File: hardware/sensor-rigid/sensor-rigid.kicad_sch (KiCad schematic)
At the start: 27 parts, among them J1 Conn_01x05, U1 PCA9546APWR

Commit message: Interrupts and new flex design
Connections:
- net SDA1: now reaches FPC1.3 (SDA1), R8.1, U1.4 (SD0)
- net SCL1: now reaches R9.1, U1.5 (SC0)
- net SCL1: now also FPC1.2 (SCL1); no longer FPC1.4
- net SDA2: now reaches FPC1.7 (SDA2), R6.2, U1.6 (SD1)
- net SCL2: now reaches R7.2, U1.7 (SC1)
- net SCL2: now also FPC1.6 (SCL2); no longer FPC1.8
- net INT1: now reaches D2.3 (COM)
- net INT1: now also FPC1.4 (INT1); no longer FPC1.2
- net INT2: now reaches D3.3 (COM)
- net INT2: now also FPC1.8 (INT2); no longer FPC1.6
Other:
- moved on the sheet: FPC1

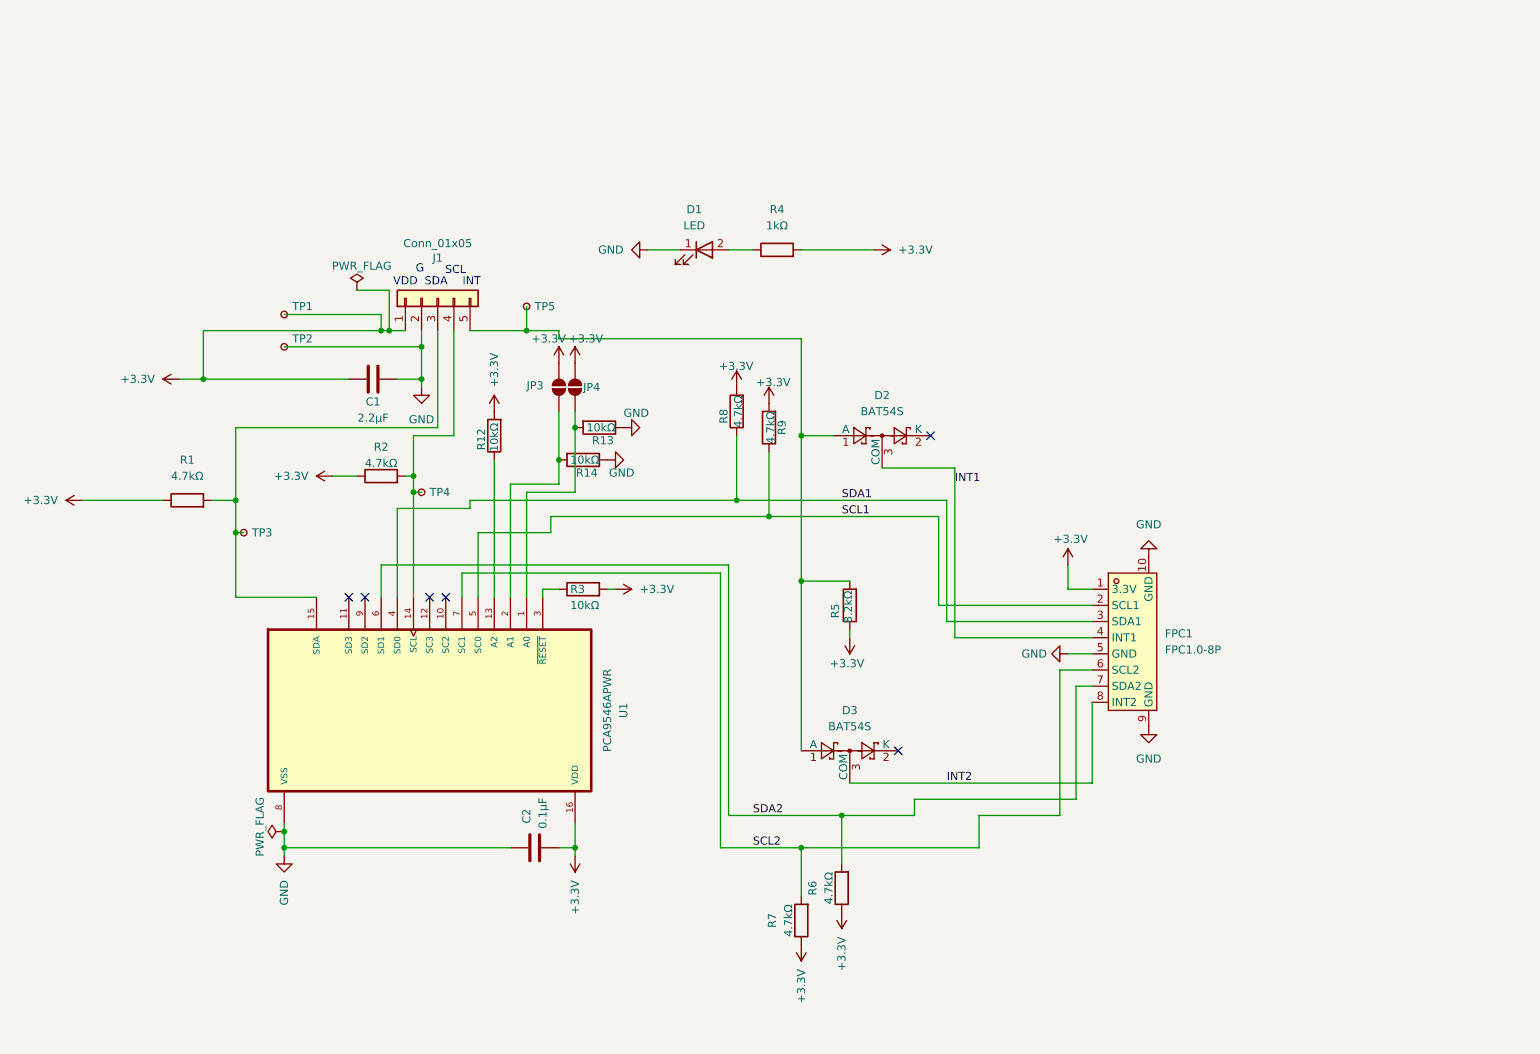
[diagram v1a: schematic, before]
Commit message: Generate circuit-context.json for sensor-rigid and sensor-flex PCBs
Run the existing schematic context extraction and annotation tooling on
both sensor board schematics. Sensor-rigid: 27 components, 16 nets,
6 functional blocks (i2c_mux, connectors, i2c_pull_ups, interrupts,
power, test_points). Sensor-flex: 9 components, 12 nets, 4 blocks
(sensor_1, sensor_2, power, connector). All ai_ properties written to
.kicad_sch files for persistence. Initiative docs and status updates
included.

Made-with: Cursor
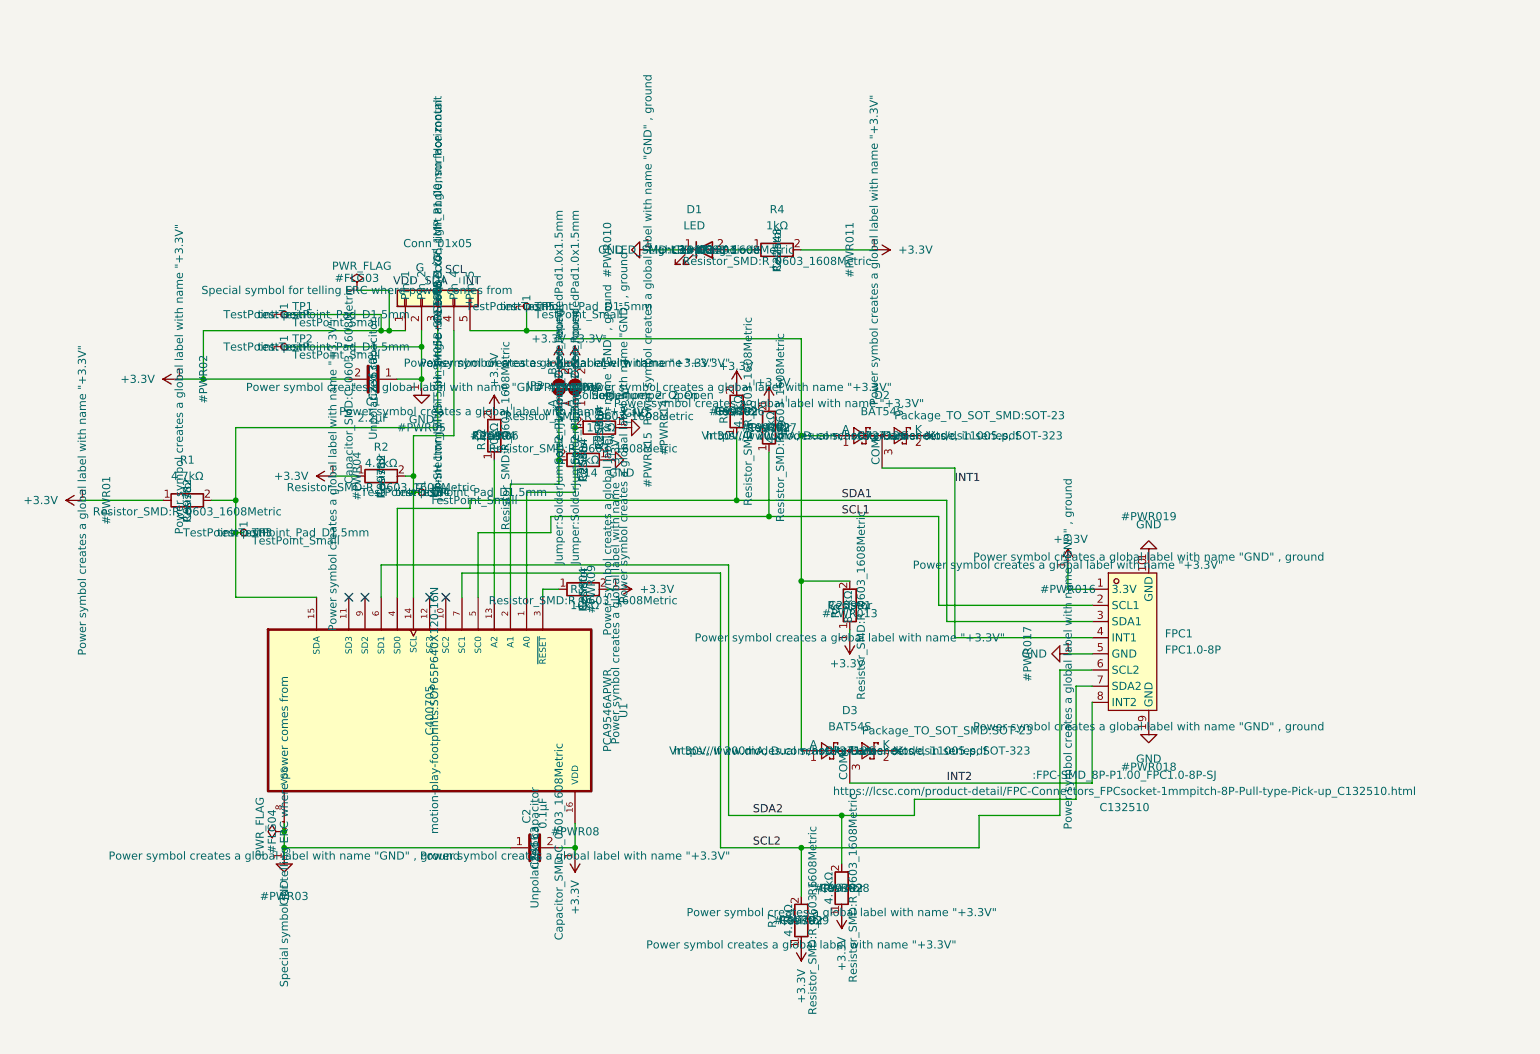
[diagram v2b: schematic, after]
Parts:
- C1: ai_block (none) -> power; ai_critical_specs (none) -> 2.2µF, 0603; ai_function (none) -> Main VDD bypass capacitor; ai_role (none) -> bypass
- C2: ai_block (none) -> power; ai_critical_specs (none) -> 0.1µF, 0603; ai_function (none) -> High-frequency bypass capacitor; ai_role (none) -> bypass
- D1: ai_block (none) -> power; ai_function (none) -> Power indicator LED; ai_role (none) -> indicator
- D2: ai_block (none) -> interrupts; ai_critical_specs (none) -> BAT54S dual Schottky, 200mA; ai_function (none) -> Wired-OR interrupt combiner for sensor 1; ai_role (none) -> diode
- D3: ai_block (none) -> interrupts; ai_critical_specs (none) -> BAT54S dual Schottky, 200mA; ai_function (none) -> Wired-OR interrupt combiner for sensor 2; ai_role (none) -> diode
- FPC1: ai_block (none) -> connectors; ai_critical_specs (none) -> 10-pin, 1.0mm pitch, top contact, slide lock; ai_function (none) -> ZIF FPC connector to flex sensor strip carrying 2x I2C, 2x 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; ai_role (none) -> connector
- J1: ai_block (none) -> connectors; ai_critical_specs (none) -> JST-SH 1mm pitch, 5-pin; ai_function (none) -> 5-pin JST-SH connector to main PCB carrying I2C, power, and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; ai_role (none) -> connector
- JP3: ai_block (none) -> i2c_mux; ai_function (none) -> A1 address select solder jumper — bridge to set A1=1; ai_role (none) -> address_config
- JP4: ai_block (none) -> i2c_mux; ai_function (none) -> A0 address select solder jumper — bridge to set A0=1; ai_role (none) -> address_config
- R1: ai_block (none) -> i2c_pull_ups; ai_critical_specs (none) -> 4.7kΩ to 3.3V; ai_function (none) -> Upstream SDA bus pull-up; ai_role (none) -> pull_up
- R12: ai_block (none) -> i2c_mux; ai_critical_specs (none) -> 10kΩ to 3.3V; ai_function (none) -> A2 address bit pull-up (A2=1 permanent); ai_role (none) -> pull_up
- R13: ai_block (none) -> i2c_mux; ai_critical_specs (none) -> 10kΩ to GND; ai_function (none) -> A0 default pull-down (A0=0 unless JP4 bridged); ai_role (none) -> pull_down
- R14: ai_block (none) -> i2c_mux; ai_critical_specs (none) -> 10kΩ to GND; ai_function (none) -> A1 default pull-down (A1=0 unless JP3 bridged); ai_role (none) -> pull_down
- R2: ai_block (none) -> i2c_pull_ups; ai_critical_specs (none) -> 4.7kΩ to 3.3V; ai_function (none) -> Upstream SCL bus pull-up; ai_role (none) -> pull_up
- R3: ai_block (none) -> i2c_mux; ai_critical_specs (none) -> 10kΩ to 3.3V; ai_function (none) -> Reset pull-up keeping PCA9546A in active state; ai_role (none) -> pull_up
- R4: ai_block (none) -> power; ai_critical_specs (none) -> 1kΩ, ~2.3mA at 3.3V; ai_function (none) -> LED current limiting resistor; ai_role (none) -> current_limit
- R5: ai_block (none) -> interrupts; ai_critical_specs (none) -> 8.2kΩ to 3.3V; ai_function (none) -> Combined INT line pull-up; ai_role (none) -> pull_up
- R6: ai_block (none) -> i2c_pull_ups; ai_critical_specs (none) -> 4.7kΩ to 3.3V; ai_function (none) -> Sensor 2 SDA downstream pull-up; ai_role (none) -> pull_up
- R7: ai_block (none) -> i2c_pull_ups; ai_critical_specs (none) -> 4.7kΩ to 3.3V; ai_function (none) -> Sensor 2 SCL downstream pull-up; ai_role (none) -> pull_up
- R8: ai_block (none) -> i2c_pull_ups; ai_critical_specs (none) -> 4.7kΩ to 3.3V; ai_function (none) -> Sensor 1 SDA downstream pull-up; ai_role (none) -> pull_up
- R9: ai_block (none) -> i2c_pull_ups; ai_critical_specs (none) -> 4.7kΩ to 3.3V; ai_function (none) -> Sensor 1 SCL downstream pull-up; ai_role (none) -> pull_up
- TP1: ai_block (none) -> test_points; ai_function (none) -> 3.3V power rail test point; ai_role (none) -> test_point
- TP2: ai_block (none) -> test_points; ai_function (none) -> GND test point; ai_role (none) -> test_point
- TP3: ai_block (none) -> test_points; ai_function (none) -> Upstream SDA bus test point; ai_role (none) -> test_point
- TP4: ai_block (none) -> test_points; ai_function (none) -> Upstream SCL bus test point; ai_role (none) -> test_point
- TP5: ai_block (none) -> test_points; ai_function (none) -> Combined INT line test point; ai_role (none) -> test_point
- U1: ai_block (none) -> i2c_mux; ai_critical_specs (none) -> PCA9546APWR, 400kHz, address set by A0-A2; ai_function (none) -> 4-channel I2C mux routing upstream bus to 2 downstream sens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; ai_role (none) -> i2c_mux

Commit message: Hardware revision: remove interrupts, update connectors, add DIP switch
Remove INT lines from all three PCBs (main, rigid, flex). Replace 5-pin
JST-SH connectors with 4-pin SM04B-SRSS-TB on main and rigid boards.
Replace solder jumpers with EP-02KS DIP switch for I2C address config
on rigid board. Update FPC connector pinout to remove INT signals and
add GND fills. Update stiffener specs (PI 0.25mm tail, SS 0.2mm IC
areas). Regenerate production files (BOM, CPL) for both sensor boards.
Update hardware CONTEXT.md with corrected addresses (0x74-0x76),
component tables, and pinouts.

Made-with: Cursor
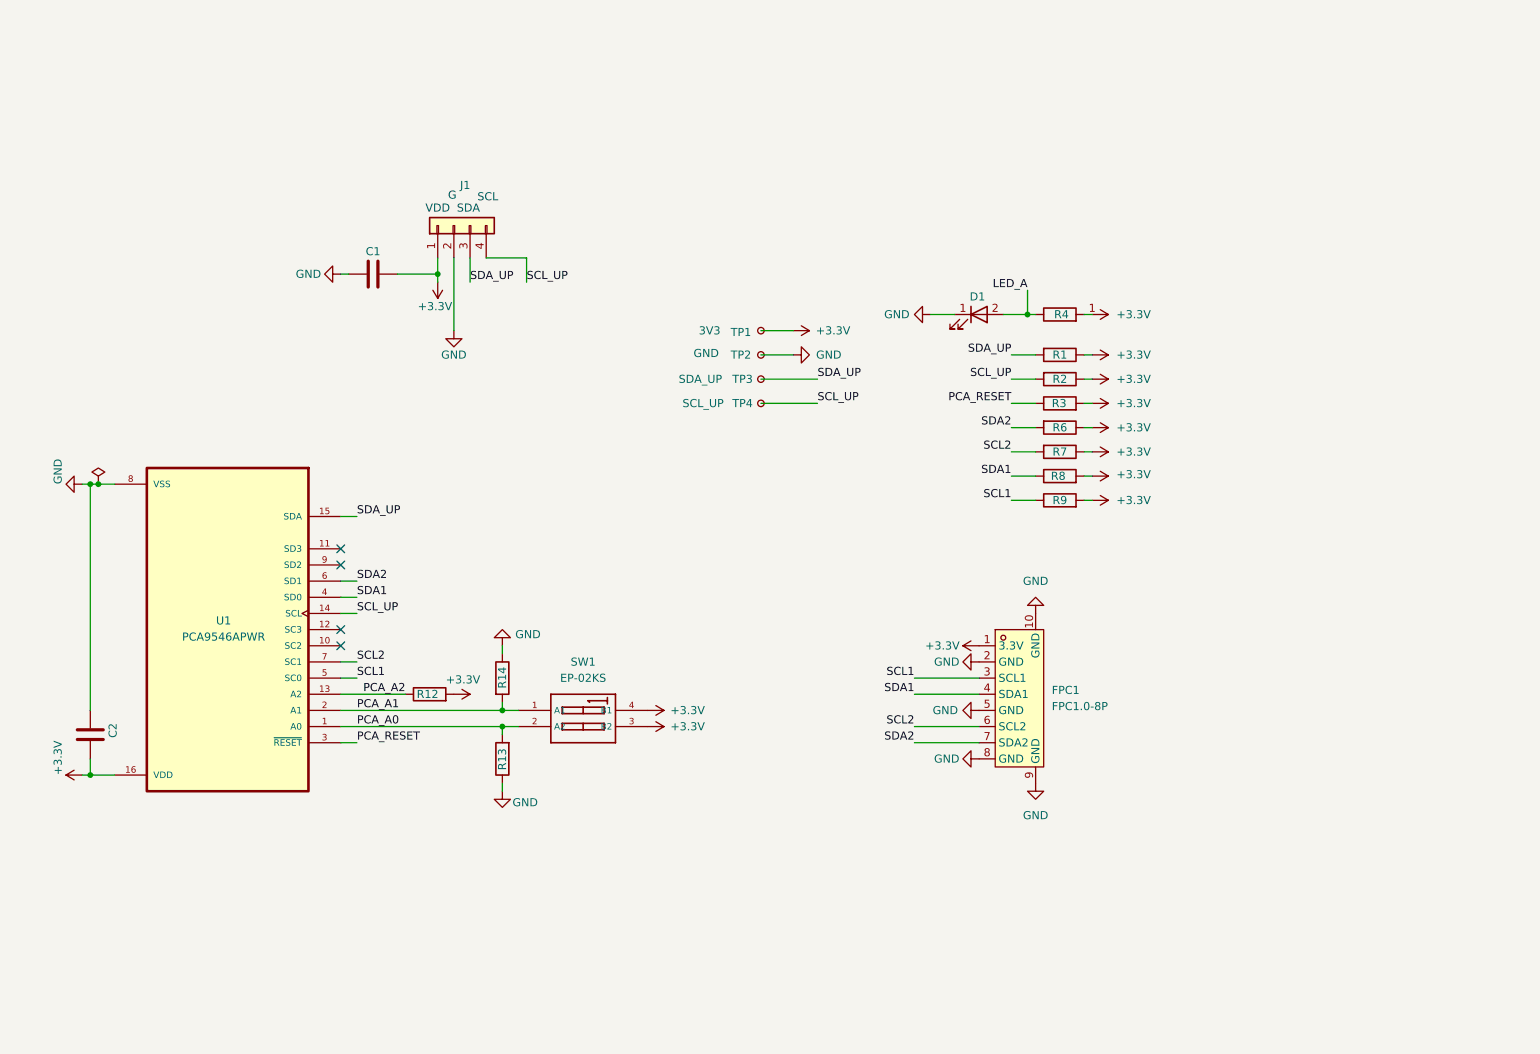
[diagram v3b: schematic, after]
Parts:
- removed D2, D3: BAT54S, Package_TO_SOT_SMD:SOT-23, symbol Diode:BAT54S
- removed JP3, JP4: SolderJumper_2_Open, Jumper:SolderJumper-2_P1.3mm_Open_RoundedPad1.0x1.5mm, symbol Jumper:SolderJumper_2_Open
- removed R5: 8.2kΩ, Resistor_SMD:R_0603_1608Metric, symbol Device:R
- removed TP5: TestPoint_Small, TestPoint:TestPoint_Pad_D1.5mm, symbol Connector:TestPoint_Small
- added SW1: EP-02KS, JLC-MCP:SW-SMD_EP-02KS, symbol JLC-MCP-Misc:EP-02KS
- J1: value Conn_01x05 -> Conn_01x04; footprint Connector_JST:JST_SH_SM05B-SRSS-TB_1x05-1MP_P1.00mm_Horizontal -> Connector_JST:JST_SH_SM04B-SRSS-TB_1x04-1MP_P1.00mm_Horizontal; symbol Connector_Generic:Conn_01x05 -> Connector_Generic:Conn_01x04; LCSC Part C136657 -> C160404; ai_critical_specs JST-SH 1mm pitch, 5-pin -> JST-SH 1mm pitch, 4-pin; ai_function 5-pin JST-SH connector to main PCB carrying I2C, power, and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 -> 4-pin JST-SH connector to main PCB carrying I2C, power
- TP1: value TestPoint_Small -> 3V3
- TP2: value TestPoint_Small -> GND
- TP3: value TestPoint_Small -> SDA_UP
- TP4: value TestPoint_Small -> SCL_UP
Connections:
- net INT1 is gone; now on net SDA1: FPC1.4 (SDA1)
- net INT2 is gone; now on net GND: FPC1.8 (GND)
- net +3.3V: now also SW1.3 (B2), SW1.4 (B1)
- net GND: now also FPC1.2 (GND)
- net SCL1: now also FPC1.3 (SCL1); no longer FPC1.2 (SCL1)
- net SDA1: no longer FPC1.3 (SDA1)
- net SCL_UP: now reaches J1.4 (Pin_4), R2.2, TP4.1, U1.14 (SCL)
- net PCA_A2: now reaches R12.1, U1.13 (A2)
- net SDA_UP: now reaches J1.3 (Pin_3), R1.2, TP3.1, U1.15 (SDA)
- net PCA_A0: now reaches R13.2, U1.1 (A0)
- net PCA_A0: now also SW1.2 (A2)
- net PCA_A1: now reaches R14.2, U1.2 (A1)
- net PCA_A1: now also SW1.1 (A1)
- net PCA_RESET: now reaches R3.1, U1.3 (~{RESET})
- net LED_A: now reaches D1.2 (A), R4.1
- no-connect marks 6 -> 4
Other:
- note removed: "INT"
- moved on the sheet: FPC1, U1
